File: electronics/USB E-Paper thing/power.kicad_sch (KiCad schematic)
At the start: 24 parts, among them J6 USB 2.0 right angle, J8 POWER_MEASUREMENT, Q2 AO3401A, U2 USBLC6-2SC6, U3 TP4056, U4 ME6216 3V0

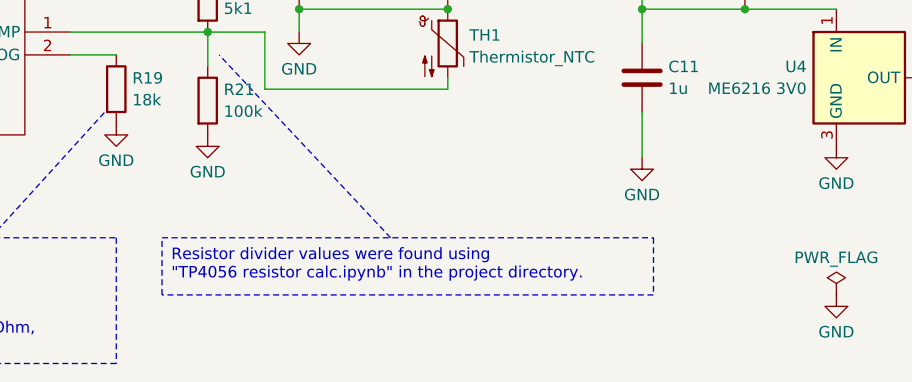
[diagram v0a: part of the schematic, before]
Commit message: add adapter board
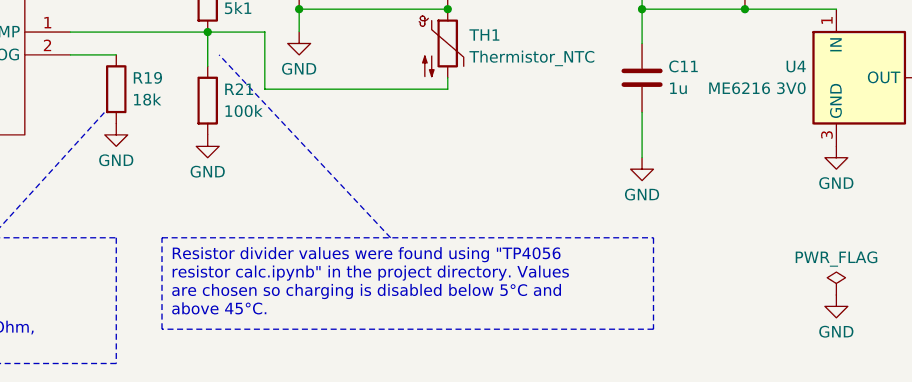
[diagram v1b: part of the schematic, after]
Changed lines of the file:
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@@
     (effects (font (size 1.27 1.27)) (justify left top))
   )
-  (text_box "Resistor divider values were found using\n\"TP4056 resistor calc.ipynb\" in the project directory."
-    (at 179.07 139.7 0) (size 54.61 6.35)
+  (text_box "Resistor divider values were found using \"TP4056 resistor calc.ipynb\" in the project directory. Values are chosen so charging is disabled below 5°C and above 45°C."
+    (at 179.07 139.7 0) (size 54.61 10.16)
     (stroke (width 0) (type dot))
     (fill (type none))

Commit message: fix TP4056 footprint
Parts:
- U3: footprint Package_SO:SOP-8-1EP_4.57x4.57mm_P1.27mm_EP4.57x4.45mm -> local:ESOP-8_L4.9-W3.9-P1.27-LS6.0-BL-EP
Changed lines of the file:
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@@
       (effects (font (size 1.27 1.27)))
     )
-    (property "Footprint" "Package_SO:SOP-8-1EP_4.57x4.57mm_P1.27mm_EP4.57x4.45mm" (at 157.48 130.81 0)
+    (property "Footprint" "local:ESOP-8_L4.9-W3.9-P1.27-LS6.0-BL-EP" (at 157.48 130.81 0)
       (effects (font (size 1.27 1.27)) hide)
     )
